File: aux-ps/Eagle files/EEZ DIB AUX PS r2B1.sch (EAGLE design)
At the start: 113 parts, among them IC1 AMC6821SDBQR, IC2 VIPer35L, IC3 TL431, J1 PF0030/PC, J2 1-726388-2, J3 1-726388-2, J4 1-726388-2, J5 SWEB 8094 AU/GN, Q1 BTA26-600, Q2 BTA26-600, Q3 2N7002, Q4 2N7002, Q5 BSP716NH6327XTSA1, Q6 2N7002, SW1 DF62J12S2AHQA, X1 39-28-1063, X2 39-30-1039, X3 ZL231-16KG, X4 22-23-2031, X5 22-23-2021

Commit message: #30, #31, #32
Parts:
- removed D7: BAS316, EEZ_Lib1:DIODESOD323R
- removed L4: ECS-MPIL0630-150MC, EEZ_inductors_and_transformers:DE0704
- removed TR1B: (WE 760875532), EEZ_Lib1:WE-UOST
- added C25: 18p, rcl:C-EUC0603
- added C26: 33n, rcl:C-EUC0805
- added C27: 2n2, rcl:C-EUC0805
- added R38: 10K, rcl:R-EU_R0805
- added R39: 6K8, rcl:R-EU_R0805
- added R40: 47K, rcl:R-EU_R0805
- added R41: 4K7, rcl:R-EU_R0805
- added X6: 22-23-2021, con-molex:22-23-2021
- added ZD4: N.C., EEZ_Lib1:ZENER-DIODESOD123
- added ZD5: BZT52C20-DC, EEZ_Lib1:ZENER-DIODESOD123
- C10: value 3n3 -> 1n/1kV; device rcl:C-EUC0805 -> rcl:C-EUC1210
- C11: value 3n3 -> UCY2G6R8MPD; device rcl:C-EUC0805 -> EEZ_Lib1:ECAP5G_10.5MM
- C12: value UVZ1C471MPD -> UCY2G6R8MPD; device EEZ_Lib1:ECAP3.5G_8MM -> EEZ_Lib1:ECAP5G_10.5MM
- C13: value 4u7 -> 3n3; device rcl:C-EUC1210 -> rcl:C-EUC0805
- C14: value EEEFK1V470P -> UVZ1C471MPD; device EEZ_Lib1:ECAPPANASONIC_H -> EEZ_Lib1:ECAP3.5G_8MM
- C15: value CY1Y-470P -> 4u7; device EEZ_Lib1:C-EUCY -> rcl:C-EUC1210
- C16: value 100n -> 3n3; device rcl:C-EUC0603 -> rcl:C-EUC0805
- C17: value 3n3 -> EEEFK1V470P; device rcl:C-EUC0805 -> EEZ_Lib1:ECAPPANASONIC_H
- C18: value 1500u/16V -> CY1Y-470P; device EEZ_Lib1:ECAP5G_13MM -> EEZ_Lib1:C-EUCY
- C19: value 4u7 -> 100n; device rcl:C-EUC1210 -> rcl:C-EUC0603
- C20: value N.C. -> 3n3
- C21: value 33n -> 1500u/16V; device rcl:C-EUC0805 -> EEZ_Lib1:ECAP5G_13MM
- C22: value 18p -> 4u7; device rcl:C-EUC0603 -> rcl:C-EUC1210
- C23: value 33n -> N.C.
- C24: value 2n2 -> 33n
- C4: value 10u -> 1u; device rcl:C-EUC1206 -> rcl:C-EUC0805
- C5: value UVZ1C471MPD -> 1u; device EEZ_Lib1:ECAP3.5G_8MM -> rcl:C-EUC0805
- C7: value 1n/1kV -> 100n; device rcl:C-EUC1210 -> rcl:C-EUC0805
- C8, C9: value UCY2G6R8MPD -> 100n; device EEZ_Lib1:ECAP5G_10.5MM -> rcl:C-EUC0603
- D1: value SKL16 -> SS110; device EEZ_Lib1:SCHOTTKYSOD123 -> EEZ_Lib1:SCHOTTKYSMB
- D2: value SS110 -> US1K-DIO; device EEZ_Lib1:SCHOTTKYSMB -> EEZ_Lib1:DIODEDO214AA
- D3: value US1K-DIO -> SS110; device EEZ_Lib1:DIODEDO214AA -> EEZ_Lib1:SCHOTTKYSMB
- D4: value SS110 -> SK55
- D5: value SK55 -> BAS316; device EEZ_Lib1:SCHOTTKYSMB -> EEZ_Lib1:DIODESOD323R
- IC1: value AMC6821SDBQR -> MAX31760AEE+; device EEZ_DIB:AMC6821 -> EEZ_DIB:MAX31760AEE+
- L1: value BLM21PG331SH1 -> RLB0812-471KL; device EEZ_Lib1:L-EU0805 -> EEZ_Lib1:FERYSTER_DSZ6
- L2: value RLB0812-471KL -> ECS-MPIL0630-150MC; device EEZ_Lib1:FERYSTER_DSZ6 -> EEZ_inductors_and_transformers:DE0704
- L3: value DLG-0403-180 -> ECS-MPIL0630-150MC; device EEZ_inductors_and_transformers:DE0403 -> EEZ_inductors_and_transformers:DE0704
- Q5: value BSP716NH6327XTSA1 -> 2N7002; device transistor-power:N-HEXFET-2D_SOT232-IRLL014N -> EEZ_Lib1:2N7002; MPN (none) -> 2N7002-7-F; OC_FARNELL (none) -> 1713823; OC_NEWARK (none) -> 25R5679; PACKAGE (none) -> SOT-23-3; SUPPLIER (none) -> DIODES INC.
- Q6: value 2N7002 -> PSMN0R9-25YLC; device EEZ_Lib1:2N7002 -> EEZ_Lib1:N-MOSFETLFPAK; MPN 2N7002-7-F -> (none); OC_FARNELL 1713823 -> (none); OC_NEWARK 25R5679 -> (none); PACKAGE SOT-23-3 -> (none); SUPPLIER DIODES INC. -> (none)
- R11: value 2K2 -> 1R
- R12: value 10K -> 470R
- R13: value 470R -> 1K
- R14: value 47K -> 1K
- R15: value 10K -> 4K7
- R16: value 4K7 -> 47K
- R17: value 2K2 -> 10R
- R18: value 220K -> 100R; device rcl:R-EU_R1206 -> rcl:R-EU_R0805
- R19: value 220K -> N.C.; device rcl:R-EU_R1206 -> rcl:R-EU_R0805
- R20: value 100K -> 10R; device rcl:R-EU_R1206 -> rcl:R-EU_R0805
- R21, R22: value 120R -> 100K; device rcl:R-EU_R0805 -> rcl:R-EU_R1206
- R23, R28: value 1K -> 100K; device rcl:R-EU_R0805 -> rcl:R-EU_R1206
- R24: value 100K -> 120R; device rcl:R-EU_R1206 -> rcl:R-EU_R0805
- R25: value 22R -> 100K; device rcl:R-EU_R0805 -> rcl:R-EU_R1206
- R26: value 100K -> 1K; device rcl:R-EU_R1206 -> rcl:R-EU_R0805
- R27: value 120R -> 22R
- R29: value N.C. -> 120R
- R30: value 4K87 -> 120R
- R31: value 10K -> 1K
- R32: value 47K -> 4K7
- R33: value 10K -> N.C.
- R34: value 6K8 -> 10K
- R35: value 1K8 -> 47K
- R36: value 47K -> 270R
- R37: value 4K7 -> 1K8
- X4: value 22-23-2031 -> 47053-1000; device con-molex:22-23-2031 -> EEZ_connectors:47053-1000
- X5: value 22-23-2021 -> 47053-1000; device con-molex:22-23-2021 -> EEZ_connectors:47053-1000
- ZD3: value BZT52C20-DC -> N.C.
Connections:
- removed net +12V_FAN: C3.1, C5.+, D1.C, L1.1, R12.2, X4-1.S
- removed net FAN_SENSE: R12.1, R15.2, X4-3.S
- removed net N$58: IC1.PWM-OUT, Q5.G, R11.2
- new net DRAIN: C7.1, Q6.D, R11.1
- new net FAN_SENSE1: R13.1, R17.2, X4-3.S, ZD4.C
- new net FAN_SENSE2: R14.1, R20.2, X5-3.S, ZD3.C
- new net N$15: C7.2, Q6.G, R18.2
- new net N$17: R21.2, R23.2
- new net N$21: C9.1, IC1.TACH2, R20.1
- new net N$22: R32.1, R36.2
- new net PWM_OUT: IC1.PWM, R15.2, R18.1, X4-4.S, X5-4.S
- net +12V: now also C15.1, C3.1, C5.1, L2.2, X4-2.S, X5-2.S; no longer C13.1, L1.2, L3.2
- net +12V_REC: now also C14.+, D1.C, L2.1, R24.1, R26.1; no longer C12.+, D2.C, L3.1, R21.1, R23.1
- net +3V3: now also R13.2, R14.2, R15.1, R19.2; no longer R11.1, R17.2
- net +5V: now also C22.1, L3.2, R16.1, R32.2; no longer C19.1, L4.2, R14.1, R30.2
- net +5V_REC: now also C21.+, D4.C, L3.1, R30.1; no longer C18.+, D5.C, L4.1, R27.1
- net 0V: now also C11.-, C12.-, C17.-, C19.1, C25.2, C27.2, D6.A, R37.2, R39.1, R40.2, ZD5.A; no longer C14.-, C16.1, C22.2, C24.2, C8.-, C9.-, D7.A, R34.1, R35.2, R36.2, TR1B.AUX, ZD3.A
- net 12VAC: now also C13.2, D1.A; no longer C10.2, D2.A, TR1B.S1_DOT
- net 5VAC: now also C20.2, D4.A; no longer C17.2, D5.A, TR1B.S1, TR1B.S2_DOT
- net AUX: now also C16.2, D3.A, D5.A, R33.2; no longer C11.2, D4.A, D6.A, R29.2, TR1B.AUX_DOT
- net AUX_OUT: now also C17.+, C19.2, R27.2, ZD5.C; no longer C14.+, C16.2, R25.2, ZD3.C
- net AUX_REC: now also D3.C, R27.1, R29.1; no longer D4.C, R22.1, R25.1
- net DC_BUS: now also C10.1, C12.+, L1.2, R21.1, R22.1; no longer C7.1, C9.+, L2.2, R18.1, R19.1, R20.1, TR1B.P1
- net FAN_OUT: now also C3.2, C5.2, R11.2, X4-1.S, X5-1.S; no longer C5.-, D1.A, Q5.D, X4-2.S
- net FB1: now also C26.1, R34.2; no longer C23.1, R31.2
- net GND: now also C14.-, C18.2, C21.-, C22.2, C8.2, C9.2, IC1.A2, R26.2, R41.1, ZD3.A, ZD4.A; no longer C12.-, C13.2, C18.-, C19.2, C3.2, IC1.PWM-MODE, R16.2, R23.2, R37.1, TR1B.S2
- net N$11: now also R25.2, R28.1; no longer R24.2, R26.1
- net N$12: now also R31.1; no longer R28.1
- net N$13: now also Q5.D, R12.2; no longer Q6.D, R13.2
- net N$137: now also C10.2, D2.C, R23.1; no longer C7.2, D3.C, R18.2, R19.2
- net N$138: now also C24.2, C27.1; no longer C21.2, C24.1
- net N$14: now also R12.1; no longer R13.1
- net N$140: now also C16.1, R29.2; no longer C11.1, R22.2
- net N$141: now also C25.1, R33.1, R35.1, R39.2; no longer C22.1, R29.1, R32.1, R34.2
- net N$146: now also C20.1, R30.2; no longer C17.1, R27.2
- net N$148: now also C23.2, R36.1, R38.2, R41.2; no longer C20.2, R30.1, R33.2, R37.2
- net N$149: now also C23.1, C26.2, R38.1; no longer C20.1, C23.2, R33.1
- net N$152: now also C24.1, R40.1; no longer C21.1, R36.1
- net N$155: now also D5.C, R35.2; no longer D7.C, R32.2
- net N$2: now also C8.1, IC1.TACH1, R17.1; no longer IC1.TACH, R15.1, R16.1
- net N$20: now also R28.2, R37.1; no longer R26.2, R35.1
- net N$3: now also IC1.!FF!/!FS!, R19.1; no longer IC1.!THERM, R17.1
- net N$4: now also C18.1; no longer C15.1
- net N$49: now also R22.2, R25.1; no longer R20.2, R24.1
- net N$5: now also R31.2, R34.1; no longer R28.2, R31.1
- net N$8: now also C13.1, R24.2; no longer C10.1, R21.2
- net N$9: now also C11.+, L1.1; no longer C8.+, L2.1
- net NFAULT: now also IC1.!ALERT; no longer IC1.!FAN-FAULT
- net PWR_DIR_OUT: now also Q5.G, R16.2; no longer Q6.G, R14.2
- net SSCL: now also IC1.SCL; no longer IC1.SCLK
- net TEMP1_N: now also IC1.DXN, X6-2.S; no longer IC1.IN-, X5-2.S
- net TEMP1_P: now also IC1.DXP, X6-1.S; no longer IC1.IN+, X5-1.S
- net VIPER_D: now also D2.A; no longer D3.A, TR1B.P1_DOT
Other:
- note added: "Connector for 3- or 4-pin DC 12V Fan"
- note added: "Fan control (Blue) 4"
- note added: "Fan sense (Green or Yellow) 3"
- note added: "Fan+ (Yellow or Red) 2"
- note added: "Fan- (Black) 1"
- note removed: "DC 12V Fan 3-pin connector"
- note removed: "Fan sense (Yellow) 3"
- note removed: "Fan+ (Red) 1"
- note removed: "Fan- (Black) 2"
- moved on the sheet: B1, C10, C12, C13, C14, C15, C16, C19, C20, C22, C23, C24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

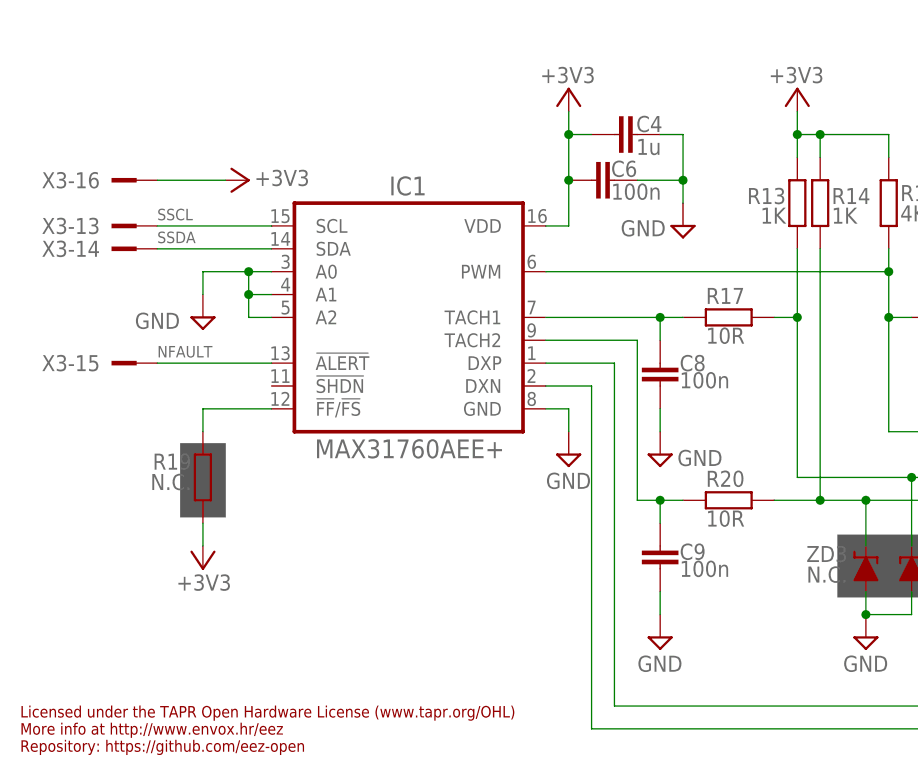
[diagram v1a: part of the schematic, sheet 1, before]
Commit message: pullup on fan controller SHDN pin, enclosure silkscreens updated
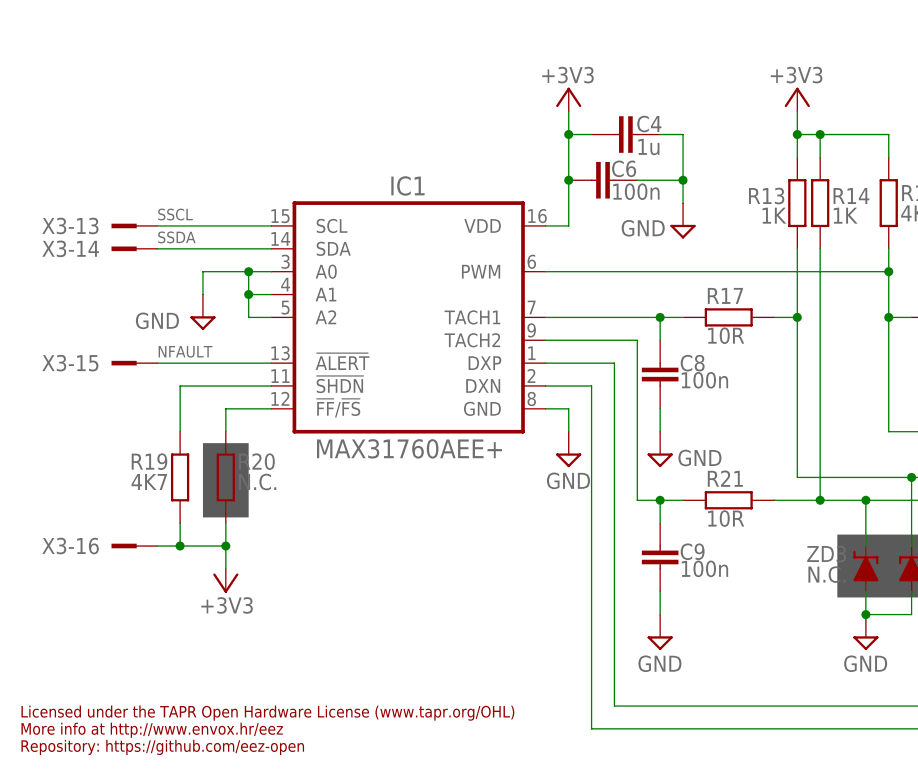
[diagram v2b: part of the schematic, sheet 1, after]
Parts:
- added R42: 4K7, rcl:R-EU_R0805
- R19, R33: value N.C. -> 4K7
- R20: value 10R -> N.C.
- R21: value 100K -> 10R; device rcl:R-EU_R1206 -> rcl:R-EU_R0805
- R24, R29: value 120R -> 100K; device rcl:R-EU_R0805 -> rcl:R-EU_R1206
- R25: value 100K -> 120R; device rcl:R-EU_R1206 -> rcl:R-EU_R0805
- R26: value 1K -> 100K; device rcl:R-EU_R0805 -> rcl:R-EU_R1206
- R27: value 22R -> 1K
- R28: value 100K -> 22R; device rcl:R-EU_R1206 -> rcl:R-EU_R0805
- R31: value 1K -> 120R
- R32: value 4K7 -> 1K
- R34: value 10K -> N.C.
- R35: value 47K -> 10K
- R36: value 270R -> 47K
- R37: value 1K8 -> 270R
- R38: value 10K -> 1K8
- R39: value 6K8 -> 10K
- R40: value 47K -> 6K8
- R41: value 4K7 -> 47K
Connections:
- new net N$18: IC1.!SHDN, R19.1
- net +12V_REC: now also R25.1, R27.1; no longer R24.1, R26.1
- net +3V3: now also R20.2
- net +5V: now also R33.2; no longer R32.2
- net +5V_REC: now also R31.1; no longer R30.1
- net 0V: now also R38.2, R40.1, R41.2; no longer R37.2, R39.1, R40.2
- net AUX: now also R34.2; no longer R33.2
- net AUX_OUT: now also R28.2; no longer R27.2
- net AUX_REC: now also R28.1, R30.1; no longer R27.1, R29.1
- net DC_BUS: now also R23.1; no longer R21.1
- net FAN_SENSE2: now also R21.2; no longer R20.2
- net FB1: now also R35.2; no longer R34.2
- net GND: now also R27.2, R42.1; no longer R26.2, R41.1
- net N$11: now also R26.2, R29.1; no longer R25.2, R28.1
- net N$12: now also R32.1; no longer R31.1
- net N$137: now also R24.1; no longer R23.1
- net N$140: now also R30.2; no longer R29.2
- net N$141: now also R34.1, R36.1, R40.2; no longer R33.1, R35.1, R39.2
- net N$146: now also R31.2; no longer R30.2
- net N$148: now also R37.1, R39.2, R42.2; no longer R36.1, R38.2, R41.2
- net N$149: now also R39.1; no longer R38.1
- net N$152: now also R41.1; no longer R40.1
- net N$155: now also R36.2; no longer R35.2
- net N$17: now also R22.2, R24.2; no longer R21.2, R23.2
- net N$20: now also R29.2, R38.1; no longer R28.2, R37.1
- net N$21: now also R21.1; no longer R20.1
- net N$22: now also R33.1, R37.2; no longer R32.1, R36.2
- net N$3: now also R20.1; no longer R19.1
- net N$49: now also R23.2, R26.1; no longer R22.2, R25.1
- net N$5: now also R32.2, R35.1; no longer R31.2, R34.1
- net N$8: now also R25.2; no longer R24.2
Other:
- note added: "I2C address: 0xA0"
- note removed: "I2C address: 0x30"
- moved on the sheet: R19, R20, R22, R23, R24, R25, R26, R27, R28, R29, R30, R31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

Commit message: #30
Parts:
- C10: value 1n/1kV -> 2n2/1kV
- R27: value 1K -> 4K7
- R28: value 22R -> 10R
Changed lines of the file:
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@@
 <part name="C22" library="rcl" deviceset="C-EU" device="C1210" value="4u7"/>
 <part name="D2" library="EEZ_Lib1" deviceset="DIODE" device="DO214AA" value="US1K-DIO"/>
-<part name="C10" library="rcl" deviceset="C-EU" device="C1210" value="1n/1kV"/>
+<part name="C10" library="rcl" deviceset="C-EU" device="C1210" value="2n2/1kV"/>
 <part name="C27" library="rcl" deviceset="C-EU" device="C0805" value="2n2"/>
 <part name="R30" library="rcl" deviceset="R-EU_" device="R0805" value="120R"/>
@@
 <part name="C20" library="rcl" deviceset="C-EU" device="C0805" value="3n3"/>
 <part name="R31" library="rcl" deviceset="R-EU_" device="R0805" value="120R"/>
-<part name="R28" library="rcl" deviceset="R-EU_" device="R0805" value="22R"/>
+<part name="R28" library="rcl" deviceset="R-EU_" device="R0805" value="10R"/>
 <part name="SUPPLY80" library="supply2" deviceset="GND" device=""/>
 <part name="FRAME3" library="frames" deviceset="DINA4_L" device=""/>
@@
 <part name="R5" library="rcl" deviceset="R-EU_" device="R0805" value="47K"/>
 <part name="R10" library="rcl" deviceset="R-EU_" device="R0805" value="47K"/>
-<part name="R27" library="rcl" deviceset="R-EU_" device="R0805" value="1K"/>
+<part name="R27" library="rcl" deviceset="R-EU_" device="R0805" value="4K7"/>
 <part name="SUPPLY8" library="supply2" deviceset="GND" device=""/>
 <part name="P+3" library="supply1" deviceset="+5V" device=""/>

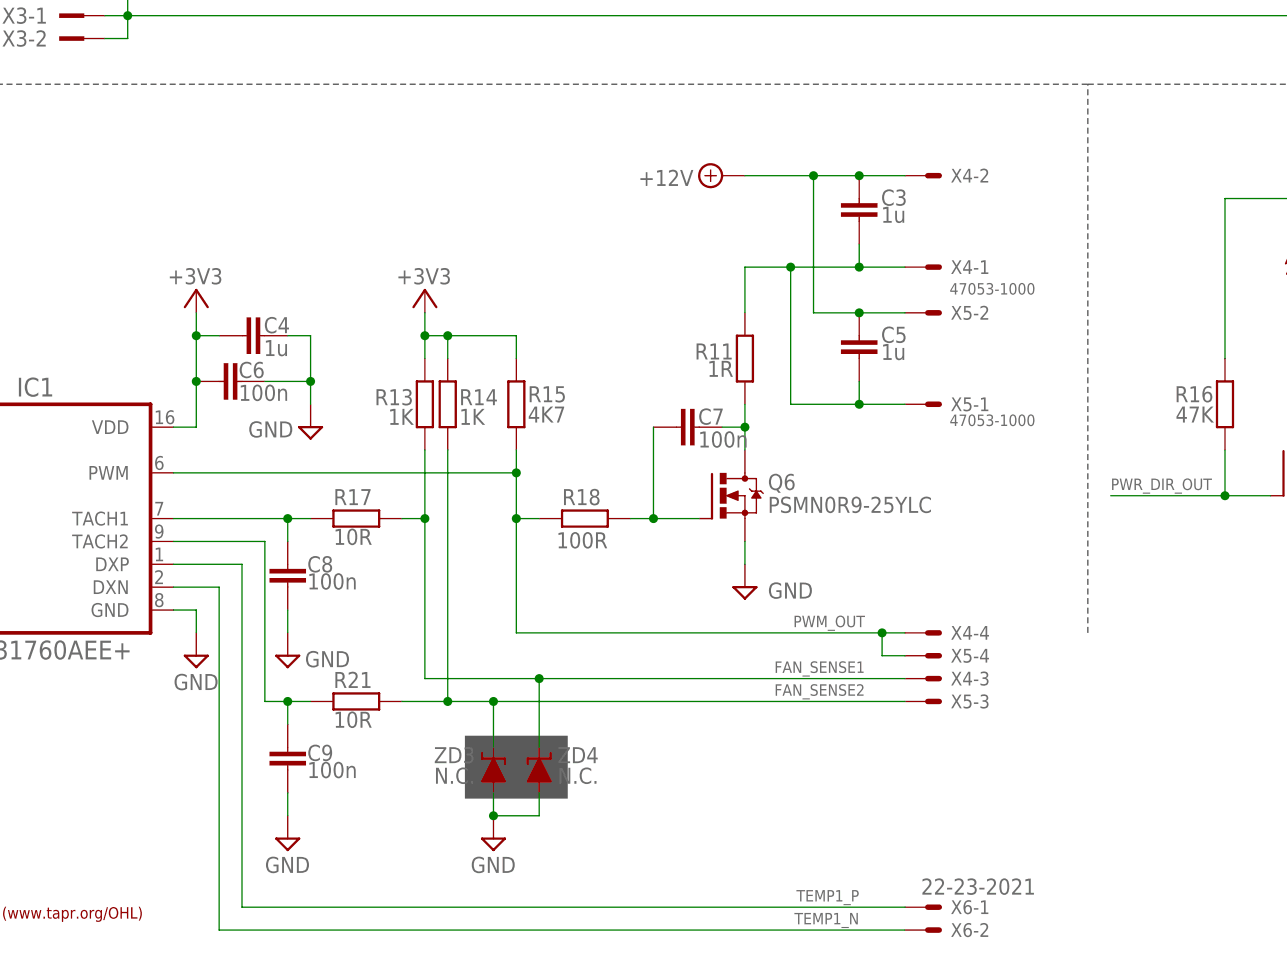
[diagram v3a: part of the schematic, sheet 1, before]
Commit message: temp. sensor C9 added
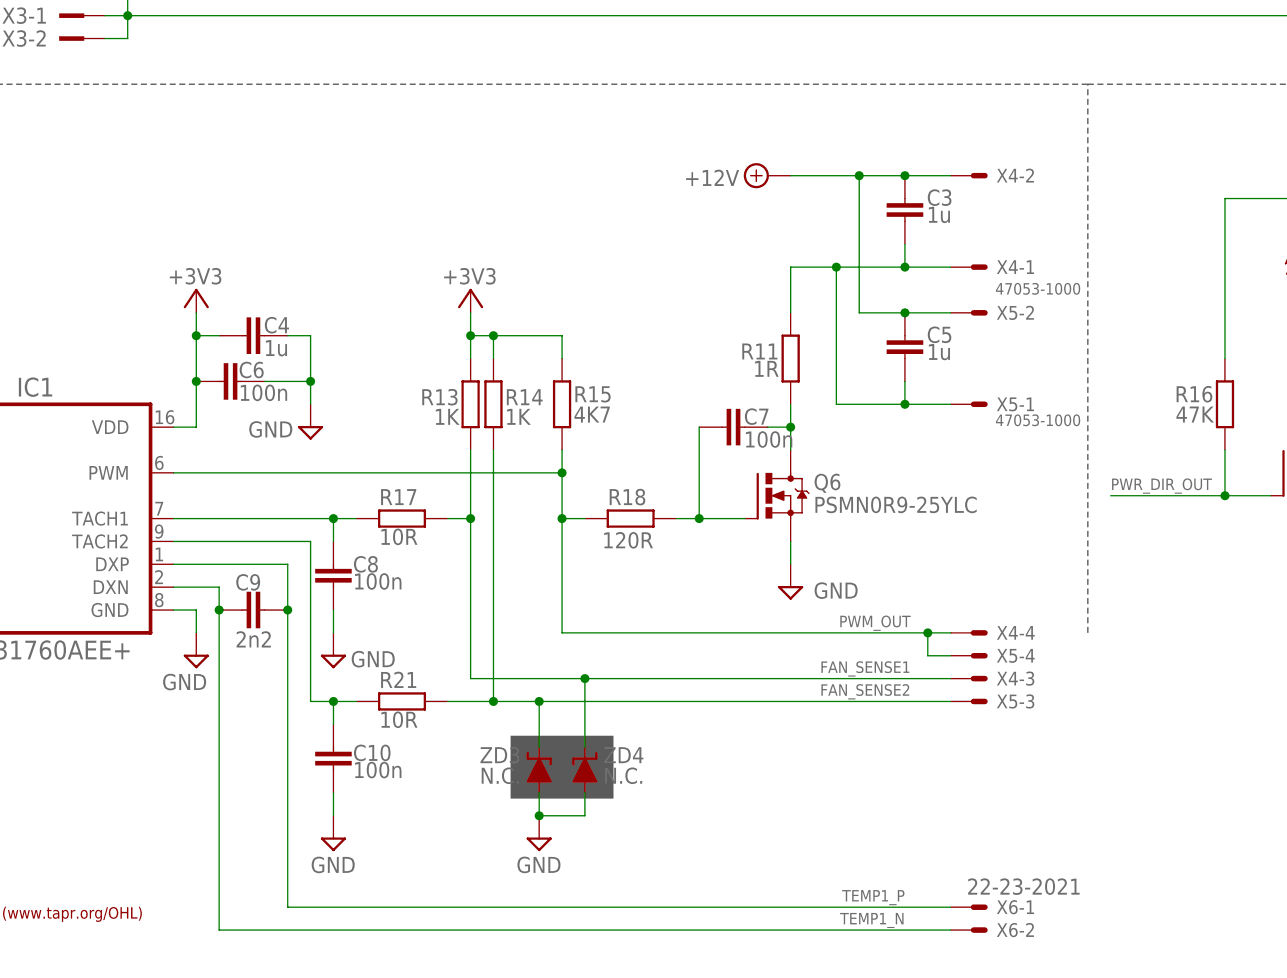
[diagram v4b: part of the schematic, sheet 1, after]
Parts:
- added C28: 2n2, rcl:C-EUC0805
- C10: value 2n2/1kV -> 100n; device rcl:C-EUC1210 -> rcl:C-EUC0603
- C11: value UCY2G6R8MPD -> 2n2/1kV; device EEZ_Lib1:ECAP5G_10.5MM -> rcl:C-EUC1210
- C13: value 3n3 -> UCY2G6R8MPD; device rcl:C-EUC0805 -> EEZ_Lib1:ECAP5G_10.5MM
- C14: value UVZ1C471MPD -> 3n3; device EEZ_Lib1:ECAP3.5G_8MM -> rcl:C-EUC0805
- C15: value 4u7 -> UVZ1C471MPD; device rcl:C-EUC1210 -> EEZ_Lib1:ECAP3.5G_8MM
- C16: value 3n3 -> 4u7; device rcl:C-EUC0805 -> rcl:C-EUC1210
- C17: value EEEFK1V470P -> 3n3; device EEZ_Lib1:ECAPPANASONIC_H -> rcl:C-EUC0805
- C18: value CY1Y-470P -> EEEFK1V470P; device EEZ_Lib1:C-EUCY -> EEZ_Lib1:ECAPPANASONIC_H
- C19: value 100n -> CY1Y-470P; device rcl:C-EUC0603 -> EEZ_Lib1:C-EUCY
- C20: value 3n3 -> 100n; device rcl:C-EUC0805 -> rcl:C-EUC0603
- C21: value 1500u/16V -> 3n3; device EEZ_Lib1:ECAP5G_13MM -> rcl:C-EUC0805
- C22: value 4u7 -> 1500u/16V; device rcl:C-EUC1210 -> EEZ_Lib1:ECAP5G_13MM
- C23: value N.C. -> 4u7; device rcl:C-EUC0805 -> rcl:C-EUC1210
- C24: value 33n -> N.C.
- C25: value 18p -> 33n; device rcl:C-EUC0603 -> rcl:C-EUC0805
- C26: value 33n -> 18p; device rcl:C-EUC0805 -> rcl:C-EUC0603
- C27: value 2n2 -> 33n
- C9: value 100n -> 2n2; device rcl:C-EUC0603 -> rcl:C-EUC0805
- R18: value 100R -> 120R
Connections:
- net +12V: now also C16.1; no longer C15.1
- net +12V_REC: now also C15.+; no longer C14.+
- net +5V: now also C23.1; no longer C22.1
- net +5V_REC: now also C22.+; no longer C21.+
- net 0V: now also C13.-, C18.-, C20.1, C26.2, C28.2; no longer C11.-, C17.-, C19.1, C25.2, C27.2
- net 12VAC: now also C14.2; no longer C13.2
- net 5VAC: now also C21.2; no longer C20.2
- net AUX: now also C17.2; no longer C16.2
- net AUX_OUT: now also C18.+, C20.2; no longer C17.+, C19.2
- net DC_BUS: now also C11.1, C13.+; no longer C10.1, C12.+
- net FB1: now also C27.1; no longer C26.1
- net GND: now also C10.2, C15.-, C16.2, C19.2, C22.-, C23.2; no longer C14.-, C15.2, C18.2, C21.-, C22.2, C9.2
- net N$137: now also C11.2; no longer C10.2
- net N$138: now also C25.2, C28.1; no longer C24.2, C27.1
- net N$140: now also C17.1; no longer C16.1
- net N$141: now also C26.1; no longer C25.1
- net N$146: now also C21.1; no longer C20.1
- net N$148: now also C24.2; no longer C23.2
- net N$149: now also C24.1, C27.2; no longer C23.1, C26.2
- net N$152: now also C25.1; no longer C24.1
- net N$21: now also C10.1; no longer C9.1
- net N$4: now also C19.1; no longer C18.1
- net N$8: now also C14.1; no longer C13.1
- net N$9: now also C12.+; no longer C11.+
- net TEMP1_N: now also C9.2
- net TEMP1_P: now also C9.1
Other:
- note added: "BD136"
- note added: "Connector for temp. sensor"
- note added: "DXN (Black) 2"
- note added: "DXP (Red) 1"
- moved on the sheet: C12, C16, C19, C20, C23, C24, C25, C26, C27, C3, C5, C7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
